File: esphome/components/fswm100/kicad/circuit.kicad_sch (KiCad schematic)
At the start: 17 parts, among them J1 Bi-Directional 3.3V-5V Shifte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, J2 ESP32 DEVKITV1 (ESP-WROOM-32), U1 ADS1115IDGS, U2 L7805, U3 TCRT5000, U4 L7805

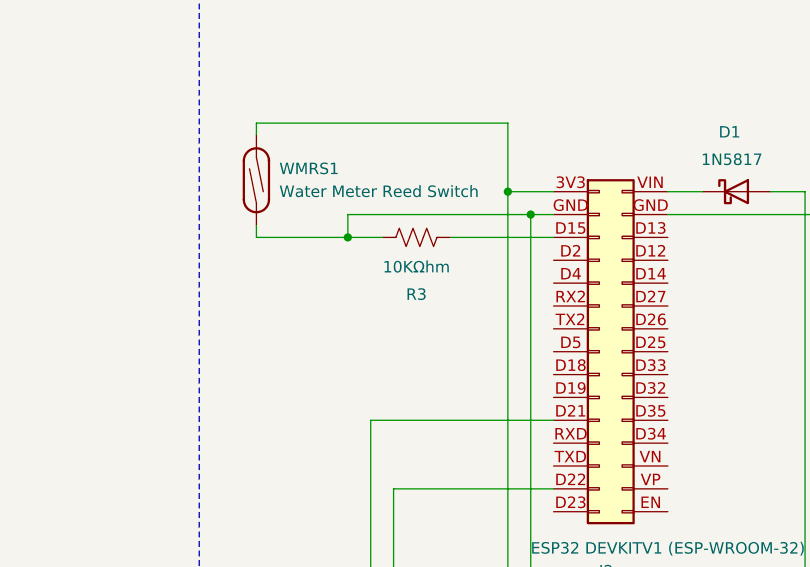
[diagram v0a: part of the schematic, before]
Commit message: change port and add circuit
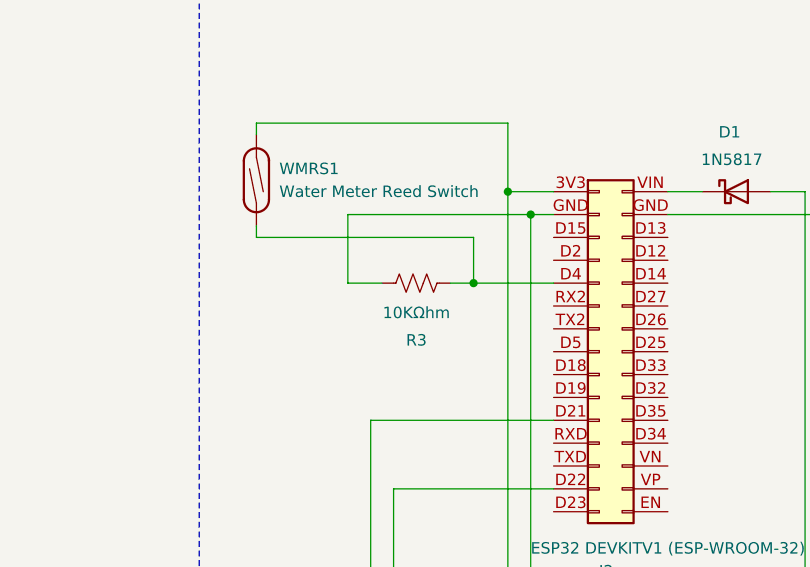
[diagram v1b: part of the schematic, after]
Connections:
- net at R3.1: now also J2.D4 (Pin_5), WMRS1.1; no longer J2.D15 (Pin_3)
- new net: J1.GND (Pin_4), J2.GND (Pin_2), R3.2
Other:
- moved on the sheet: R3
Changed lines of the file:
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@@
 	(title_block
 		(title "FSWM100")
-		(date "2025-02-26")
-		(rev "1.0.0")
+		(date "2025-04-13")
+		(rev "1.0.1")
 		(company "Antonios Karagiannis")
 		(comment 1 "both L7805 need heatsinks 25x34x12mm+")
@@
 	)
 	(junction
-		(at 210.82 64.77)
-		(diameter 0)
-		(color 0 0 0 0)
-	)
-	(junction
 		(at 140.97 71.12)
 		(diameter 0)
@@
 	)
 	(junction
+		(at 224.79 69.85)
+		(diameter 0)
+		(color 0 0 0 0)
+	)
+	(junction
 		(at 66.04 74.93)
 		(diameter 0)
@@
 	(wire
 		(pts
+			(xy 224.79 69.85) (xy 233.68 69.85)
+		)
+		(stroke
+			(width 0)
+			(type default)
+		)
+	)
+	(wire
+		(pts
 			(xy 90.17 59.69) (xy 104.14 59.69)
 		)
@@
 	(wire
 		(pts
-			(xy 222.25 64.77) (xy 233.68 64.77)
-		)
-		(stroke
-			(width 0)
-			(type default)
-		)
-	)
-	(wire
-		(pts
 			(xy 179.07 130.81) (xy 170.18 130.81)
 		)
@@
 	(wire
 		(pts
+			(xy 200.66 64.77) (xy 224.79 64.77)
+		)
+		(stroke
+			(width 0)
+			(type default)
+		)
+	)
+	(wire
+		(pts
 			(xy 157.48 45.72) (xy 90.17 45.72)
 		)
@@
 	(wire
 		(pts
-			(xy 210.82 64.77) (xy 200.66 64.77)
-		)
-		(stroke
-			(width 0)
-			(type default)
-		)
-	)
-	(wire
-		(pts
 			(xy 49.53 63.5) (xy 58.42 63.5)
 		)
@@
 	(wire
 		(pts
+			(xy 222.25 69.85) (xy 224.79 69.85)
+		)
+		(stroke
+			(width 0)
+			(type default)
+		)
+	)
+	(wire
+		(pts
 			(xy 158.75 99.06) (xy 170.18 99.06)
 		)
@@
 	(wire
 		(pts
-			(xy 210.82 62.23) (xy 210.82 64.77)
-		)
-		(stroke
-			(width 0)
-			(type default)
-		)
-	)
-	(wire
-		(pts
 			(xy 231.14 133.35) (xy 231.14 62.23)
 		)
@@
 	(wire
 		(pts
-			(xy 214.63 64.77) (xy 210.82 64.77)
+			(xy 214.63 69.85) (xy 210.82 69.85)
 		)
 		(stroke
@@
 	(wire
 		(pts
+			(xy 210.82 62.23) (xy 210.82 69.85)
+		)
+		(stroke
+			(width 0)
+			(type default)
+		)
+	)
+	(wire
+		(pts
 			(xy 205.74 151.13) (xy 214.63 151.13)
 		)
@@
 		(pts
 			(xy 90.17 99.06) (xy 90.17 93.98)
+		)
+		(stroke
+			(width 0)
+			(type default)
+		)
+	)
+	(wire
+		(pts
+			(xy 224.79 64.77) (xy 224.79 69.85)
 		)
 		(stroke
@@
 	(symbol
 		(lib_id "Device:R_US")
-		(at 218.44 64.77 270)
+		(at 218.44 69.85 270)
 		(unit 1)
 		(exclude_from_sim no)
@@
 		(dnp no)
 		(property "Reference" "R3"
-			(at 218.44 71.12 90)
+			(at 218.44 76.2 90)
 			(effects
 				(font
@@
 		)
 		(property "Value" "10KΩhm"
-			(at 218.44 68.072 90)
+			(at 218.44 73.152 90)
 			(effects
 				(font
@@
 		)
 		(property "Footprint" ""
-			(at 218.186 65.786 90)
+			(at 218.186 70.866 90)
 			(effects
 				(font
@@
 		)
 		(property "Datasheet" "~"
-			(at 218.44 64.77 0)
+			(at 218.44 69.85 0)
 			(effects
 				(font
@@
 		)
 		(property "Description" "Resistor, US symbol"
-			(at 218.44 64.77 0)
-			(effects
-				(font
+			(at 218.44 69.85 0)
+			(effects
+				(font
